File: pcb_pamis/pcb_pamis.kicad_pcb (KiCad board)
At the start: 2 copper layers, 60 x 51.5 mm, 5 parts, among them J1 1755736, U1 ESP32-WROOM-32UE

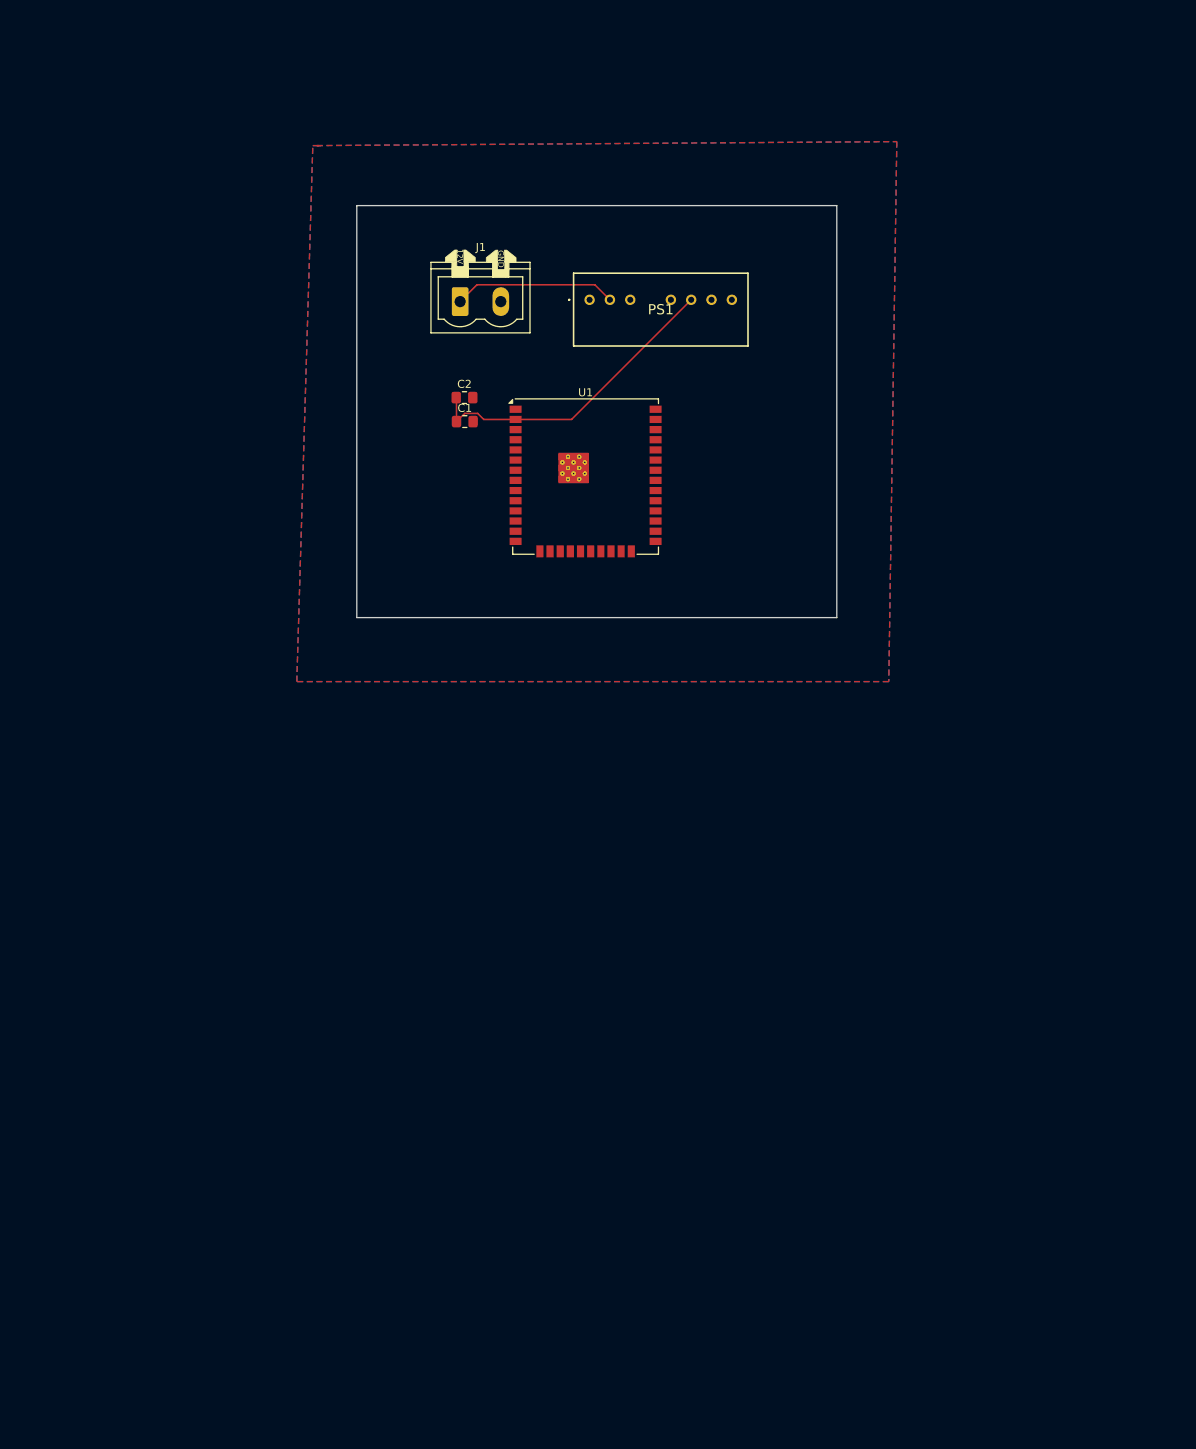
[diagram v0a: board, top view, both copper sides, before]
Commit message: finalisation empreintes des composants
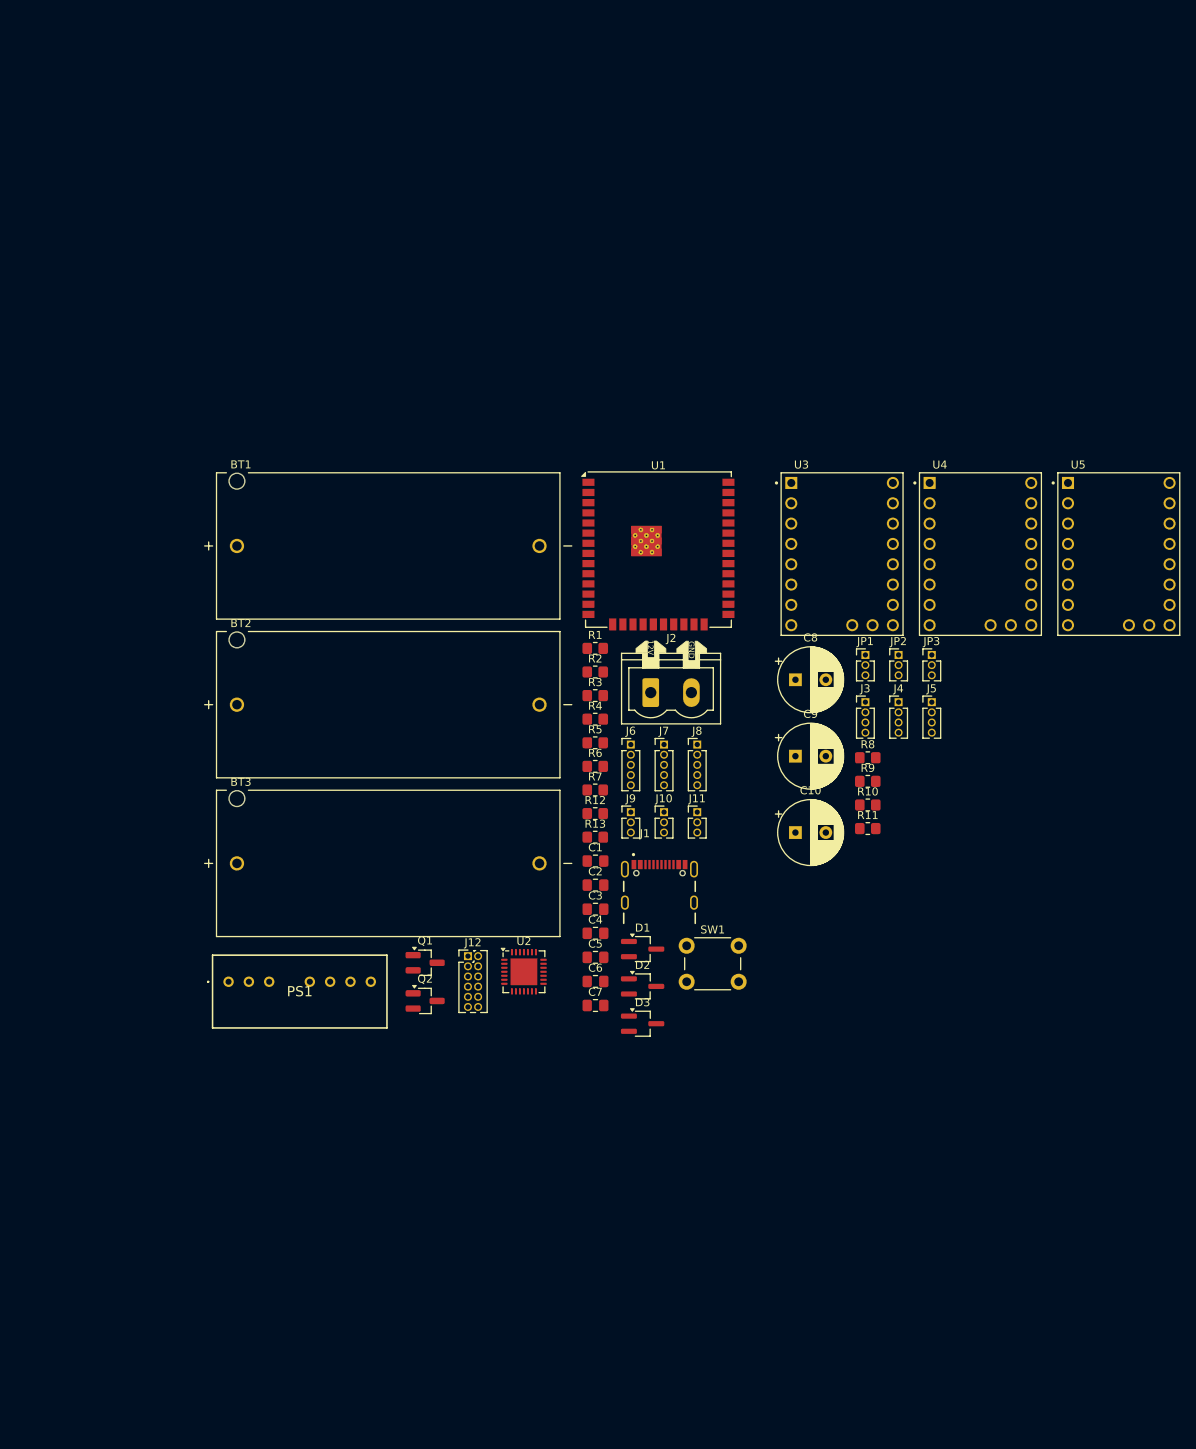
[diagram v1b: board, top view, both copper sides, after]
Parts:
- added BT1: Battery_Cell, Modelec:BAT_1051_CR123A, F.Cu at (107.4, 84.5)
- added BT2: Battery_Cell, Modelec:BAT_1051_CR123A, F.Cu at (107.4, 104.4)
- added BT3: Battery_Cell, Modelec:BAT_1051_CR123A, F.Cu at (107.4, 124.2)
- added C10: 100uF 50V, Capacitor_THT:CP_Radial_D8.0mm_P3.80mm, F.Cu at (158.3, 120.4)
- added C3: 1u, Capacitor_SMD:C_0805_2012Metric_Pad1.18x1.45mm_HandSolder, F.Cu at (133.3, 129.9)
- added C4: 10u, Capacitor_SMD:C_0805_2012Metric_Pad1.18x1.45mm_HandSolder, F.Cu at (133.3, 133.0)
- added C5: 1u, Capacitor_SMD:C_0805_2012Metric_Pad1.18x1.45mm_HandSolder, F.Cu at (133.3, 136.0)
- added C6: 10u, Capacitor_SMD:C_0805_2012Metric_Pad1.18x1.45mm_HandSolder, F.Cu at (133.3, 139.0)
- added C7: 0.1uF/50V, Capacitor_SMD:C_0805_2012Metric_Pad1.18x1.45mm_HandSolder, F.Cu at (133.3, 142.0)
- added C8: 100uF 50V, Capacitor_THT:CP_Radial_D8.0mm_P3.80mm, F.Cu at (158.3, 101.3)
- added C9: 100uF 50V, Capacitor_THT:CP_Radial_D8.0mm_P3.80mm, F.Cu at (158.3, 110.8)
- added D1: D_Dual_CommonCathode_AAK_Parallel, Package_TO_SOT_SMD:TSOT-23_HandSoldering, F.Cu at (139.2, 134.9)
- added D2: D_Dual_CommonCathode_AAK_Parallel, Package_TO_SOT_SMD:TSOT-23_HandSoldering, F.Cu at (139.2, 139.6)
- added D3: D_Dual_CommonCathode_AAK_Parallel, Package_TO_SOT_SMD:TSOT-23_HandSoldering, F.Cu at (139.2, 144.3)
- added J10: Conn_01x03, Connector_PinHeader_1.27mm:PinHeader_1x03_P1.27mm_Vertical, F.Cu at (141.9, 117.8)
- added J11: Conn_01x03, Connector_PinHeader_1.27mm:PinHeader_1x03_P1.27mm_Vertical, F.Cu at (146.1, 117.8)
- added J12: Conn_02x06_Odd_Even, Connector_PinHeader_1.27mm:PinHeader_2x06_P1.27mm_Vertical, F.Cu at (117.4, 135.8)
- added J2: 1755736, Modelec:PhoenixContact_MSTBVA_2,5_2-G-5,08_1x02_P5.08mm_Vertical, F.Cu at (140.2, 102.9)
- added J3: Conn_01x04, Connector_PinHeader_1.27mm:PinHeader_1x04_P1.27mm_Vertical, F.Cu at (167.1, 104.1)
- added J4: Conn_01x04, Connector_PinHeader_1.27mm:PinHeader_1x04_P1.27mm_Vertical, F.Cu at (171.2, 104.1)
- added J5: Conn_01x04, Connector_PinHeader_1.27mm:PinHeader_1x04_P1.27mm_Vertical, F.Cu at (175.4, 104.1)
- added J6: Conn_01x05, Connector_PinHeader_1.27mm:PinHeader_1x05_P1.27mm_Vertical, F.Cu at (137.8, 109.4)
- added J7: Conn_01x05, Connector_PinHeader_1.27mm:PinHeader_1x05_P1.27mm_Vertical, F.Cu at (141.9, 109.4)
- added J8: Conn_01x05, Connector_PinHeader_1.27mm:PinHeader_1x05_P1.27mm_Vertical, F.Cu at (146.1, 109.4)
- added J9: Conn_01x03, Connector_PinHeader_1.27mm:PinHeader_1x03_P1.27mm_Vertical, F.Cu at (137.8, 117.8)
- added JP1: Jumper_3_Bridged12, Connector_PinHeader_1.27mm:PinHeader_1x03_P1.27mm_Vertical, F.Cu at (167.1, 98.2)
- added JP2: Jumper_3_Bridged12, Connector_PinHeader_1.27mm:PinHeader_1x03_P1.27mm_Vertical, F.Cu at (171.2, 98.2)
- added JP3: Jumper_3_Bridged12, Connector_PinHeader_1.27mm:PinHeader_1x03_P1.27mm_Vertical, F.Cu at (175.4, 98.2)
- added Q1: Q_NPN_BEC, Package_TO_SOT_SMD:SOT-23_Handsoldering, F.Cu at (112.0, 136.6)
- added Q2: Q_NPN_BEC, Package_TO_SOT_SMD:SOT-23_Handsoldering, F.Cu at (112.0, 141.4)
- added R1: 470R, Resistor_SMD:R_0805_2012Metric_Pad1.20x1.40mm_HandSolder, F.Cu at (133.3, 97.3)
- added R10: 10K, Resistor_SMD:R_0805_2012Metric_Pad1.20x1.40mm_HandSolder, F.Cu at (167.4, 116.9)
- added R11: 10K, Resistor_SMD:R_0805_2012Metric_Pad1.20x1.40mm_HandSolder, F.Cu at (167.4, 119.9)
- added R12: 2k2, Resistor_SMD:R_0805_2012Metric_Pad1.20x1.40mm_HandSolder, F.Cu at (133.3, 118.0)
- added R13: 2k2, Resistor_SMD:R_0805_2012Metric_Pad1.20x1.40mm_HandSolder, F.Cu at (133.3, 121.0)
- added R2: 470R, Resistor_SMD:R_0805_2012Metric_Pad1.20x1.40mm_HandSolder, F.Cu at (133.3, 100.3)
- added R3: 470R, Resistor_SMD:R_0805_2012Metric_Pad1.20x1.40mm_HandSolder, F.Cu at (133.3, 103.2)
- added R4: 10K, Resistor_SMD:R_0805_2012Metric_Pad1.20x1.40mm_HandSolder, F.Cu at (133.3, 106.2)
- added R5: 10K, Resistor_SMD:R_0805_2012Metric_Pad1.20x1.40mm_HandSolder, F.Cu at (133.3, 109.2)
- added R6: 10k, Resistor_SMD:R_0805_2012Metric_Pad1.20x1.40mm_HandSolder, F.Cu at (133.3, 112.1)
- added R7: 10k/1%, Resistor_SMD:R_0805_2012Metric_Pad1.20x1.40mm_HandSolder, F.Cu at (133.3, 115.0)
- added R8: 1K, Resistor_SMD:R_0805_2012Metric_Pad1.20x1.40mm_HandSolder, F.Cu at (167.4, 111.0)
- added R9: 10K, Resistor_SMD:R_0805_2012Metric_Pad1.20x1.40mm_HandSolder, F.Cu at (167.4, 114.0)
- added SW1: SW_Push, Button_Switch_THT:SW_PUSH_6mm_H4.3mm, F.Cu at (144.7, 134.5)
- added U2: CP2102N-Axx-xQFN28, Package_DFN_QFN:QFN-28-1EP_5x5mm_P0.5mm_EP3.35x3.35mm, F.Cu at (124.4, 137.8)
- added U3: TMC2209_SILENTSTEPSTICK, Modelec:MODULE_TMC2209_SILENTSTEPSTICK, F.Cu at (164.2, 85.6)
- added U4: TMC2209_SILENTSTEPSTICK, Modelec:MODULE_TMC2209_SILENTSTEPSTICK, F.Cu at (181.5, 85.6)
- added U5: TMC2209_SILENTSTEPSTICK, Modelec:MODULE_TMC2209_SILENTSTEPSTICK, F.Cu at (198.8, 85.6)
- C2: value 10u -> 22u
- J1: value 1755736 -> USB_A; footprint Modelec:PhoenixContact_MSTBVA_2,5_2-G-5,08_1x02_P5.08mm_Vertical -> Modelec:GCT_USB4105-GF-A
- moved PS1 96.5 mm to (87.5, 139.0)
- moved J1 79.1 mm to (141.3, 129.1)
- moved C2 63.1 mm to (133.3, 126.9)
- moved C1 57.3 mm to (133.3, 123.9)
- moved U1 12.9 mm to (141.2, 85.0)
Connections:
- PS1 pad 2: Net-(PS1-+VIN_(VCC)) -> VCC
- U1 pad 10: unconnected-(U1-IO25-Pad10) -> STEP3
- U1 pad 11: unconnected-(U1-IO26-Pad11) -> DISA1
- U1 pad 12: unconnected-(U1-IO27-Pad12) -> DISA2
- U1 pad 13: unconnected-(U1-IO14-Pad13) -> GPIO14/CLK
- U1 pad 14: unconnected-(U1-IO12-Pad14) -> GPIO12/MISO
- U1 pad 16: unconnected-(U1-IO13-Pad16) -> GPIO13/MOSI
- U1 pad 23: unconnected-(U1-IO15-Pad23) -> GPIO15/CS
- U1 pad 24: unconnected-(U1-IO2-Pad24) -> GPIO2
- U1 pad 25: unconnected-(U1-IO0-Pad25) -> IO0
- U1 pad 26: unconnected-(U1-IO4-Pad26) -> GPIO4
- U1 pad 27: unconnected-(U1-IO16-Pad27) -> RX_MOTEUR
- U1 pad 28: unconnected-(U1-IO17-Pad28) -> TX_MOTEUR
- U1 pad 29: unconnected-(U1-IO5-Pad29) -> GPIO5
- U1 pad 3: unconnected-(U1-EN-Pad3) -> EN
- U1 pad 30: unconnected-(U1-IO18-Pad30) -> DIR1
- U1 pad 31: unconnected-(U1-IO19-Pad31) -> DIR2
- U1 pad 33: unconnected-(U1-IO21-Pad33) -> DIR3
- U1 pad 34: unconnected-(U1-RXD0/IO3-Pad34) -> RXD
- U1 pad 35: unconnected-(U1-TXD0/IO1-Pad35) -> TXD
- U1 pad 36: unconnected-(U1-IO22-Pad36) -> STEP1
- U1 pad 37: unconnected-(U1-IO23-Pad37) -> STEP2
- U1 pad 6: unconnected-(U1-IO34-Pad6) -> SDA
- U1 pad 7: unconnected-(U1-IO35-Pad7) -> SCL
- U1 pad 8: unconnected-(U1-IO32-Pad8) -> DISA3
- U1 pad 9: unconnected-(U1-IO33-Pad9) -> GPIO33
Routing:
- net +3.3V: track 39.3 -> 0.00 mm
- net Net-(PS1-+VIN_(VCC)): track 20.4 -> 0.00 mm
- removed copper zone on B.Cu, net GND
- removed copper zone on F.Cu, net GND
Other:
- board outline removed

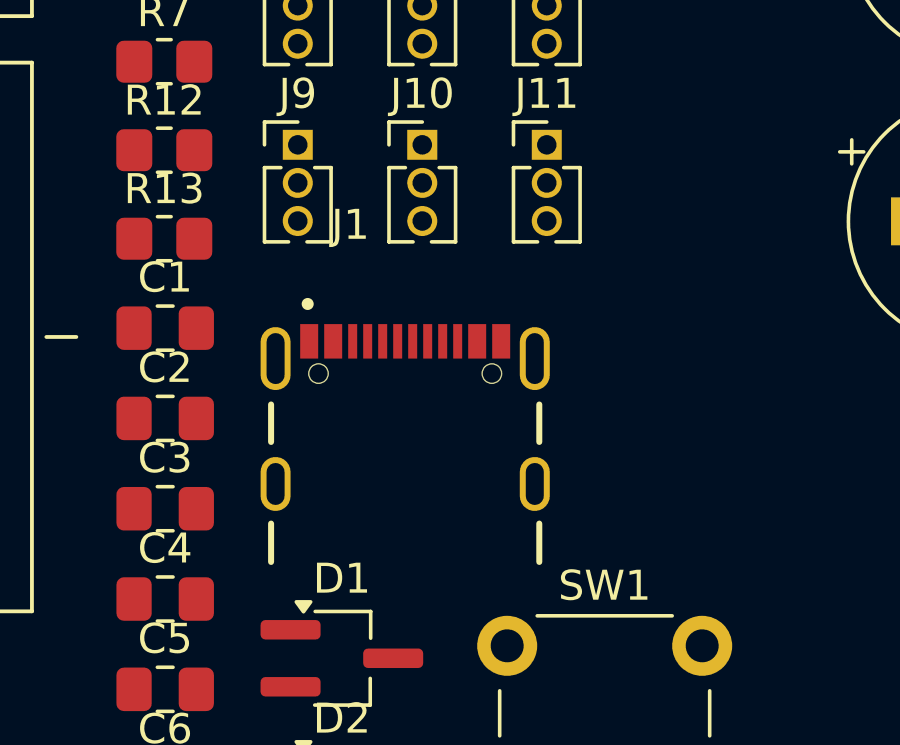
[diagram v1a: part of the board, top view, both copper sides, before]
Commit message: remplacement usb A par type C sur schéma PAMI pour une meilleure cohérence avec le PCB
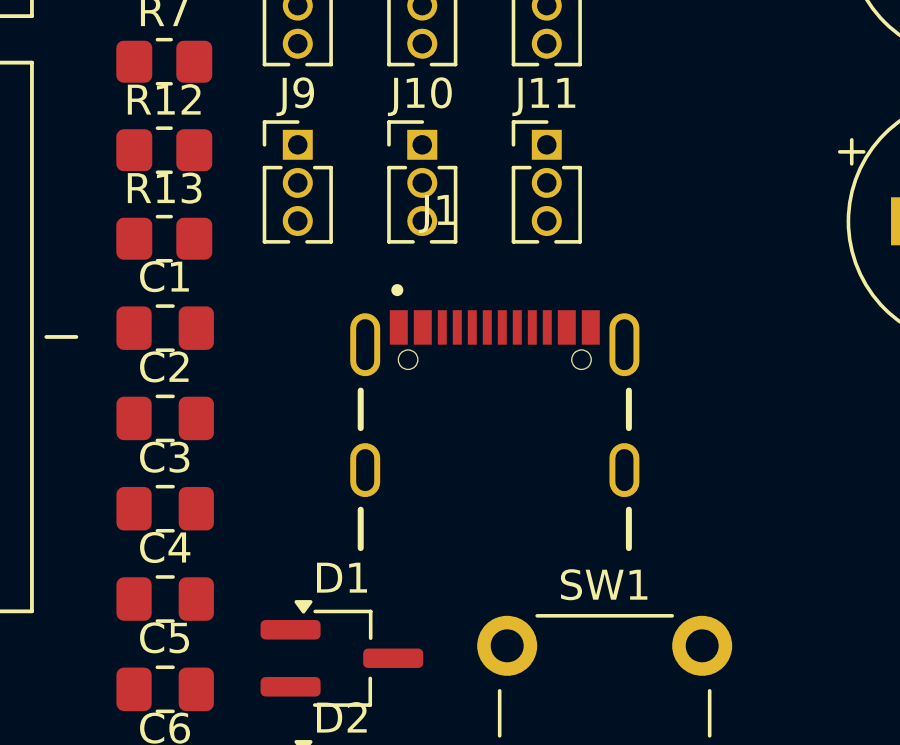
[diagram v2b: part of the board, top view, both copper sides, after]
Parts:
- moved J1 3.02 mm to (144.3, 128.7)
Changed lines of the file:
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@@
 	(footprint "Modelec:GCT_USB4105-GF-A"
 		(layer "F.Cu")
-		(at 141.335 129.125)
+		(at 144.3225 128.6625)
 		(descr "Connecteur USB-C")
 		(property "Reference" "J1"
